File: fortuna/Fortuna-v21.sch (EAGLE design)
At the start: 33 parts, among them J1 9V, M1 MOTOR20MM, M2 MOTOR20MM, Q1 600mA/40V, Q2 600mA/40V, U2 OPA2344, U3 OPA2344

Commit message: Design board layout for Fortuna - v2.1
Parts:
- removed B1: ARDUINO_UNO_R3, SparkFun-Boards:ARDUINO_UNO_R3
- removed U3: OPA2344, Texas Instruments_By_element14_Batch_1:OPA2343UA
- added G1: AB9V, battery:AB9V
- added J2: GND, SparkFun-Connectors:CONN_01
- added J3: A0, SparkFun-Connectors:CONN_01
- added J4: A3, SparkFun-Connectors:CONN_01
- added J5: A5, SparkFun-Connectors:CONN_01
- added J6: D2, SparkFun-Connectors:CONN_01
- added J7: *D5, SparkFun-Connectors:CONN_01
- added J8: *D10, SparkFun-Connectors:CONN_01
- added J9: VIN, SparkFun-Connectors:CONN_01
- added U1: OPA2344, TexasInstruments:OPA2277PA
- D3: value LLED -> LLED_RED; device SparkFun-LED:LED3MM -> SparkFun-LED:LED5MM
- D4: value RLED -> RLED_RED; device SparkFun-LED:LED3MM -> SparkFun-LED:LED5MM
- J1: value 9V -> 5V; device SparkFun-Connectors:BC9VPC -> SparkFun-Connectors:CONN_01
- M1, M2: device SparkFun-Electromechanical:MOTOR10MM -> SparkFun-Connectors:CONN_02
- Q1, Q2: value 600mA/40V -> PN2222A; device SparkFun-DiscreteSemi:TRANS_NPN-P2N2222A -> Adafruit:2N2222
- U2: device Texas Instruments_By_element14_Batch_1:OPA2343UA -> TexasInstruments:OPA2277PA
- renumbered C3 to C1
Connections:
- removed net *D11: B1.*D11
- removed net *D3: B1.*D3
- removed net *D6: B1.*D6
- removed net *D9: B1.*D9
- removed net 3.3V: B1.3.3V
- removed net A1: B1.A1
- removed net A2: B1.A2
- removed net A4: B1.A4
- removed net AREF: B1.AREF
- removed net D0(RX): B1.D0
- removed net D1(TX): B1.D1
- removed net D12: B1.D12
- removed net D13: B1.D13
- removed net D4: B1.D4
- removed net D7: B1.D7
- removed net D8: B1.D8
- removed net IOREF: B1.IOREF
- removed net MISO: B1.MISO
- removed net MOSI: B1.MOSI
- removed net RESET: B1.!RESET!@1, B1.!RESET!@2
- removed net SCK: B1.SCK
- removed net SCL: B1.SCL
- removed net SDA: B1.SDA
- removed net VCC: B1.VCC
- net *D10: now also J8.1; no longer B1.*D10
- net *D5: now also J7.1; no longer B1.*D5
- net +LPHOTO: now also U1.+IN_A; no longer U2.+IN_A
- net +MIC: now also U1.+IN_B; no longer U2.+IN_B
- net +RPHOTO: now also U2.+IN_A; no longer U3.+IN_A
- net -LPHOTO: now also U1.-IN_A; no longer U2.-IN_A
- net -MIC: now also U1.-IN_B; no longer U2.-IN_B
- net -RPHOTO: now also U2.-IN_A; no longer U3.-IN_A
- net 5V: now also J1.1, U1.V+; no longer B1.5V, U3.V+
- net A0: now also J3.1, U1.OUT_A; no longer B1.A0, U2.OUT_A
- net A3: now also J4.1, U1.OUT_B; no longer B1.A3, U2.OUT_B
- net A5: now also J5.1, U2.OUT_A; no longer B1.A5, U3.OUT_A
- net D2: now also J6.1, U2.+IN_B; no longer B1.D2, U3.+IN_B
- net GND: now also G1.-, J2.1, U1.V-; no longer B1.GND, B1.GND@0, B1.GND@1, B1.GND@2, J1.V-, U3.V-
- net N$10: now also M1.2; no longer M1.-
- net N$12: now also M2.2; no longer M2.-
- net OUT_BUZZER: now also U2.-IN_B, U2.OUT_B; no longer U3.-IN_B, U3.OUT_B
- net VIN: now also G1.+, J9.1, M1.1, M2.1; no longer B1.VIN, J1.V+, M1.+, M2.+
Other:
- note added: "2.1"
- note removed: "2.0"
- moved on the sheet: U2

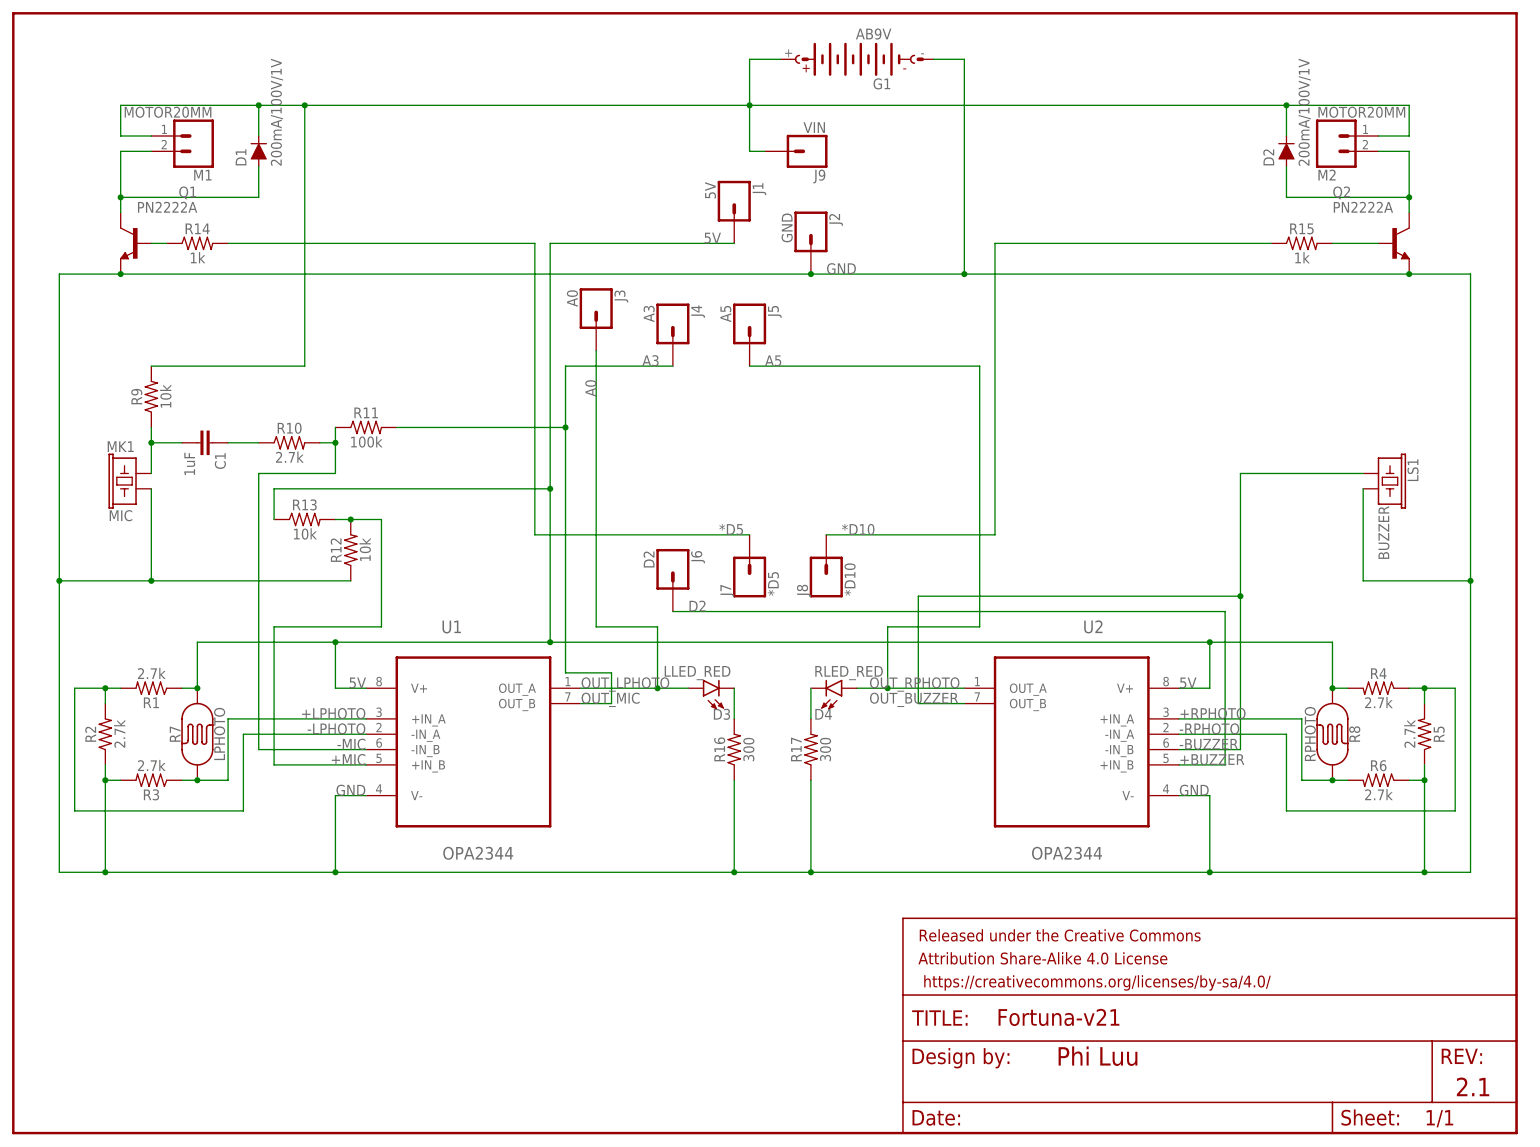
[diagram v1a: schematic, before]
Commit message: Merge two OPA2344's into one OPA4344 & Add SPDT power switch
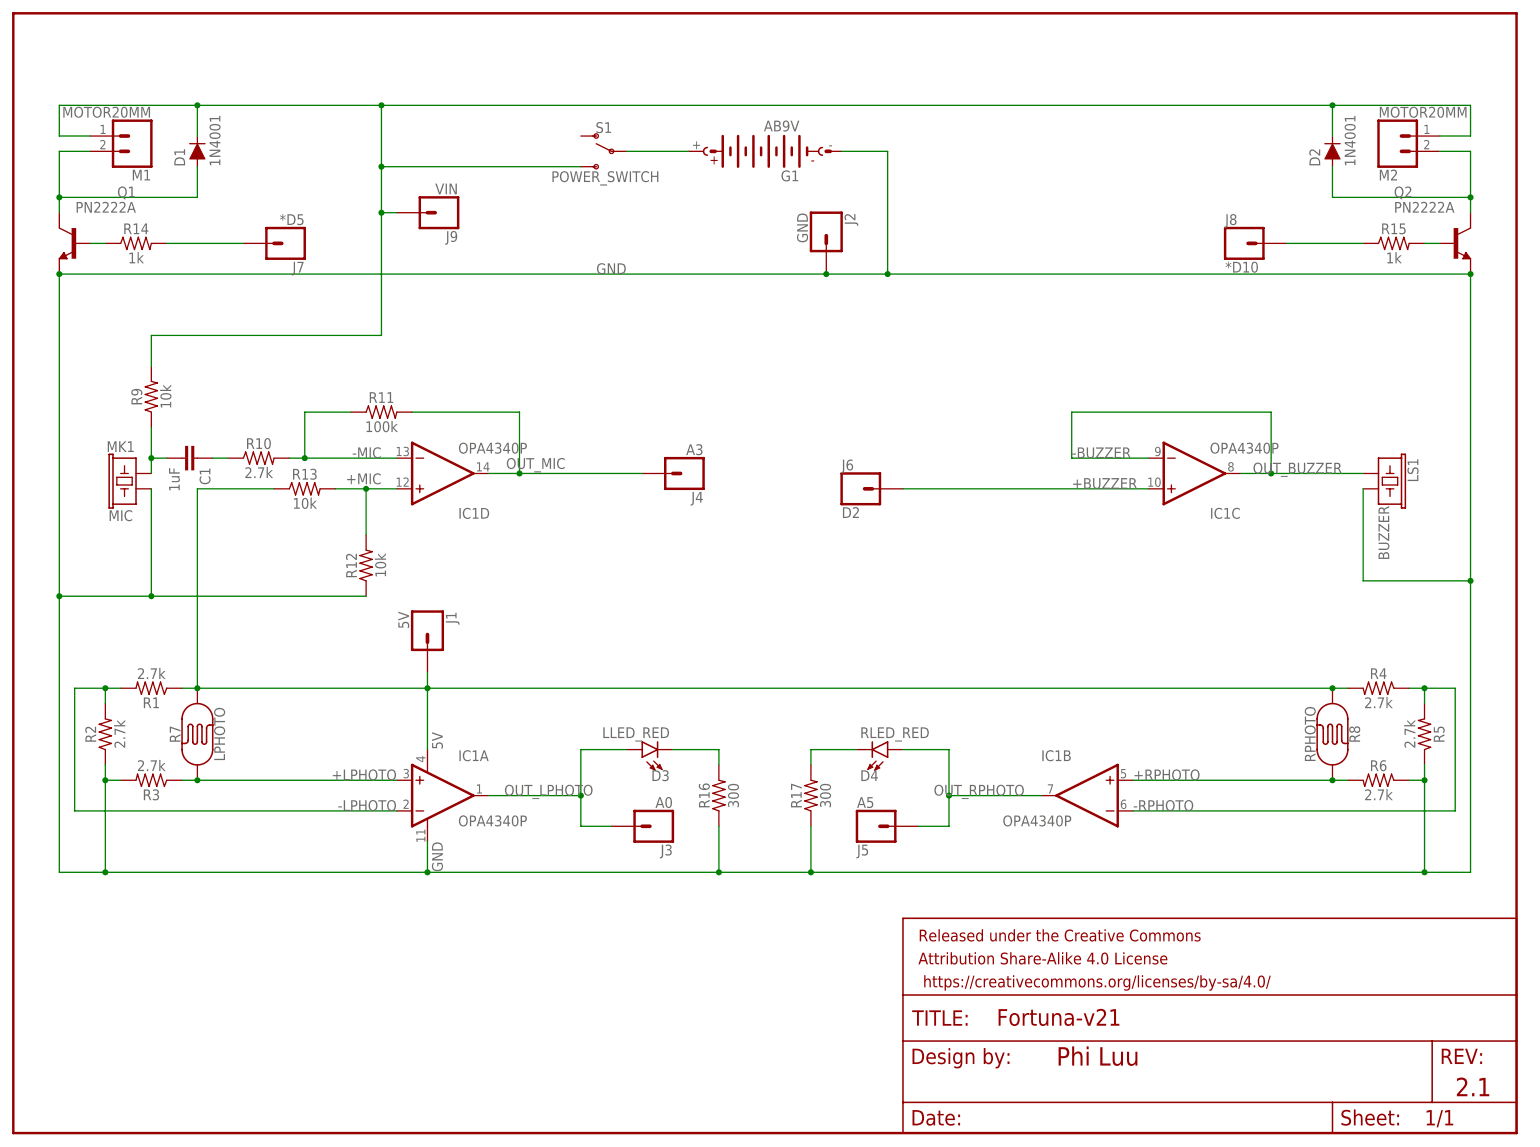
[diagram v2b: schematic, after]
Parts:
- removed U1, U2: OPA2344, TexasInstruments:OPA2277PA
- added IC1: OPA4340P, burr-brown:OPA4340P
- added S1: POWER_SWITCH, SparkFun-Switches:SWITCH-SPDT-PTH-11.6X4.0MM
- D1, D2: value 200mA/100V/1V -> 1N4001
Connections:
- net *D10 renamed OUT_RMOTOR
- net *D5 renamed OUT_LMOTOR
- removed net A0: D3.A, J3.1, U1.OUT_A
- removed net A3: J4.1, R11.2, U1.OUT_B
- removed net A5: D4.A, J5.1, U2.OUT_A
- new net 9V: G1.+, S1.P
- new net OUT_LPHOTO: D3.A, IC1A.OUT, J3.1
- new net OUT_MIC: IC1D.OUT, J4.1, R11.2
- new net OUT_RPHOTO: D4.A, IC1B.OUT, J5.1
- net +LPHOTO: now also IC1A.+IN; no longer U1.+IN_A
- net +MIC: now also IC1D.+IN; no longer U1.+IN_B
- net +RPHOTO: now also IC1B.+IN; no longer U2.+IN_A
- net -LPHOTO: now also IC1A.-IN; no longer U1.-IN_A
- net -MIC: now also IC1D.-IN; no longer U1.-IN_B
- net -RPHOTO: now also IC1B.-IN; no longer U2.-IN_A
- net 5V: now also IC1A.V+; no longer U1.V+, U2.V+
- net D2: now also IC1C.+IN; no longer U2.+IN_B
- net GND: now also IC1A.V-; no longer U1.V-, U2.V-
- net OUT_BUZZER: now also IC1C.-IN, IC1C.OUT; no longer U2.-IN_B, U2.OUT_B
- net VIN: now also S1.S; no longer G1.+
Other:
- note removed: "OUT_LPHOTO"
- note removed: "OUT_MIC"
- note removed: "OUT_RPHOTO"
- moved on the sheet: C1, D1, D2, D3, D4, G1, J1, J2, J3, J4, J5, J6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

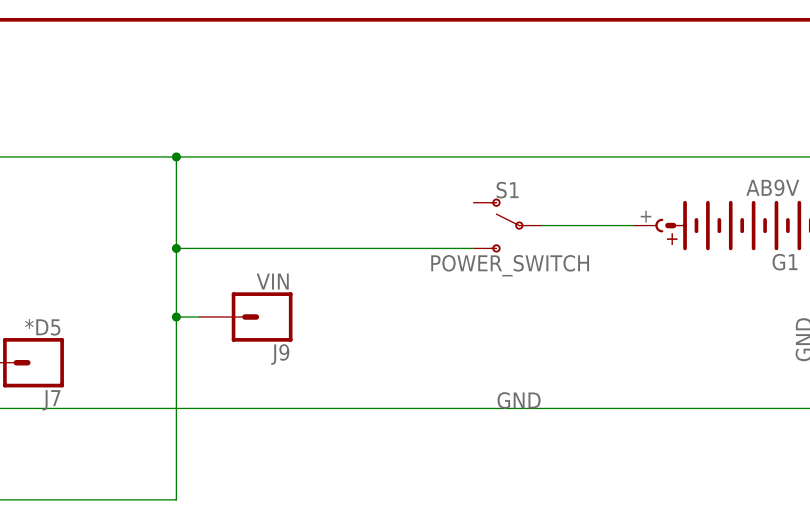
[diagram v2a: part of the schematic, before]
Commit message: Change pin position SPDT slide switch
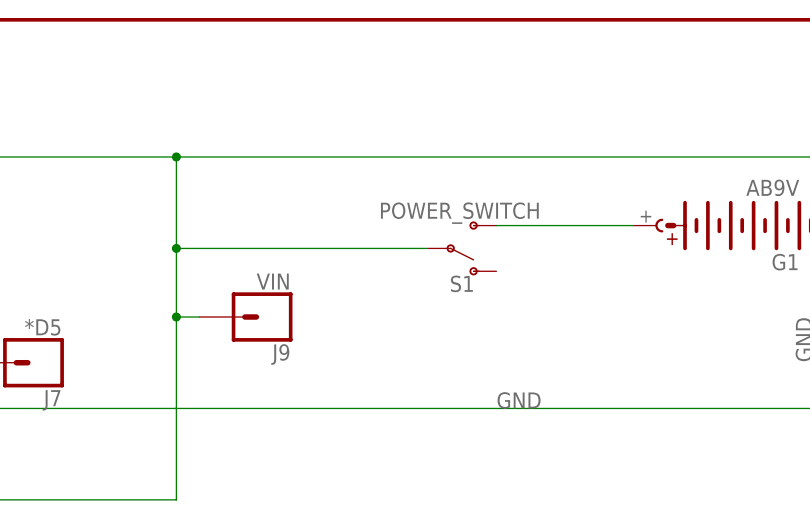
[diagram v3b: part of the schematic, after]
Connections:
- net 9V: now also S1.S; no longer S1.P
- net VIN: now also S1.P; no longer S1.S
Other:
- moved on the sheet: S1
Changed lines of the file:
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@@
 <instance part="IC1" gate="C" x="195.58" y="109.22" rot="MR180"/>
 <instance part="IC1" gate="D" x="71.12" y="109.22" rot="MR180"/>
-<instance part="S1" gate="1" x="99.06" y="162.56" rot="MR0"/>
+<instance part="S1" gate="1" x="91.44" y="160.02" rot="MR180"/>
 </instances>
 <busses>
@@
 <wire x1="60.96" y1="132.08" x2="60.96" y2="152.4" width="0.1524" layer="91"/>
 <wire x1="60.96" y1="152.4" x2="60.96" y2="160.02" width="0.1524" layer="91"/>
-<wire x1="60.96" y1="160.02" x2="93.98" y2="160.02" width="0.1524" layer="91"/>
-<pinref part="S1" gate="1" pin="S"/>
-<wire x1="60.96" y1="160.02" x2="60.96" y2="170.18" width="0.1524" layer="91"/>
-<junction x="60.96" y="160.02"/>
 <junction x="60.96" y="170.18"/>
 <pinref part="J9" gate="G$1" pin="1"/>
+<wire x1="60.96" y1="160.02" x2="60.96" y2="170.18" width="0.1524" layer="91"/>
 <wire x1="60.96" y1="152.4" x2="63.5" y2="152.4" width="0.1524" layer="91"/>
 <junction x="60.96" y="152.4"/>
+<pinref part="S1" gate="1" pin="P"/>
+<wire x1="88.9" y1="160.02" x2="60.96" y2="160.02" width="0.1524" layer="91"/>
+<junction x="60.96" y="160.02"/>
 </segment>
 </net>
@@
 </segment>
 </net>
-<net name="9V" class="1">
+<net name="9V" class="0">
 <segment>
 <pinref part="G1" gate="G$1" pin="+"/>
-<pinref part="S1" gate="1" pin="P"/>
-<wire x1="111.76" y1="162.56" x2="101.6" y2="162.56" width="0.1524" layer="91"/>
-</segment>
-</net>
+<pinref part="S1" gate="1" pin="S"/>
+<wire x1="111.76" y1="162.56" x2="96.52" y2="162.56" width="0.1524" layer="91"/>
+</segment>
+</net>

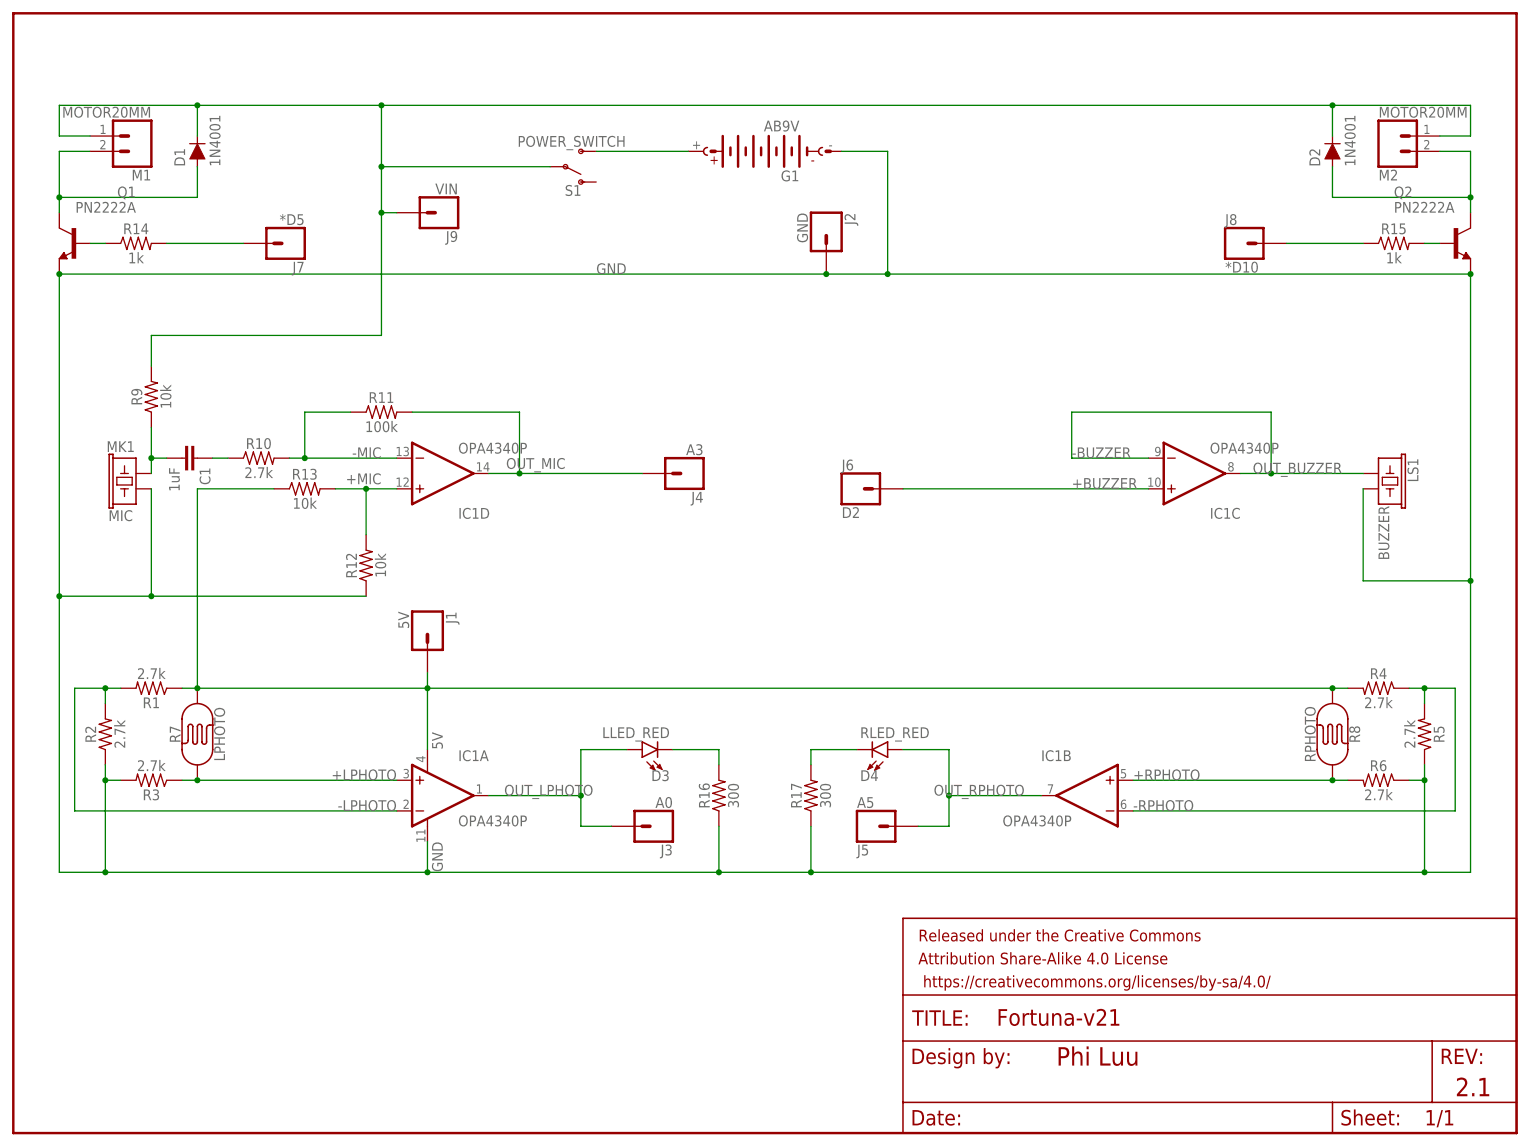
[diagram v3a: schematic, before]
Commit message: Add GND to RATSNEST
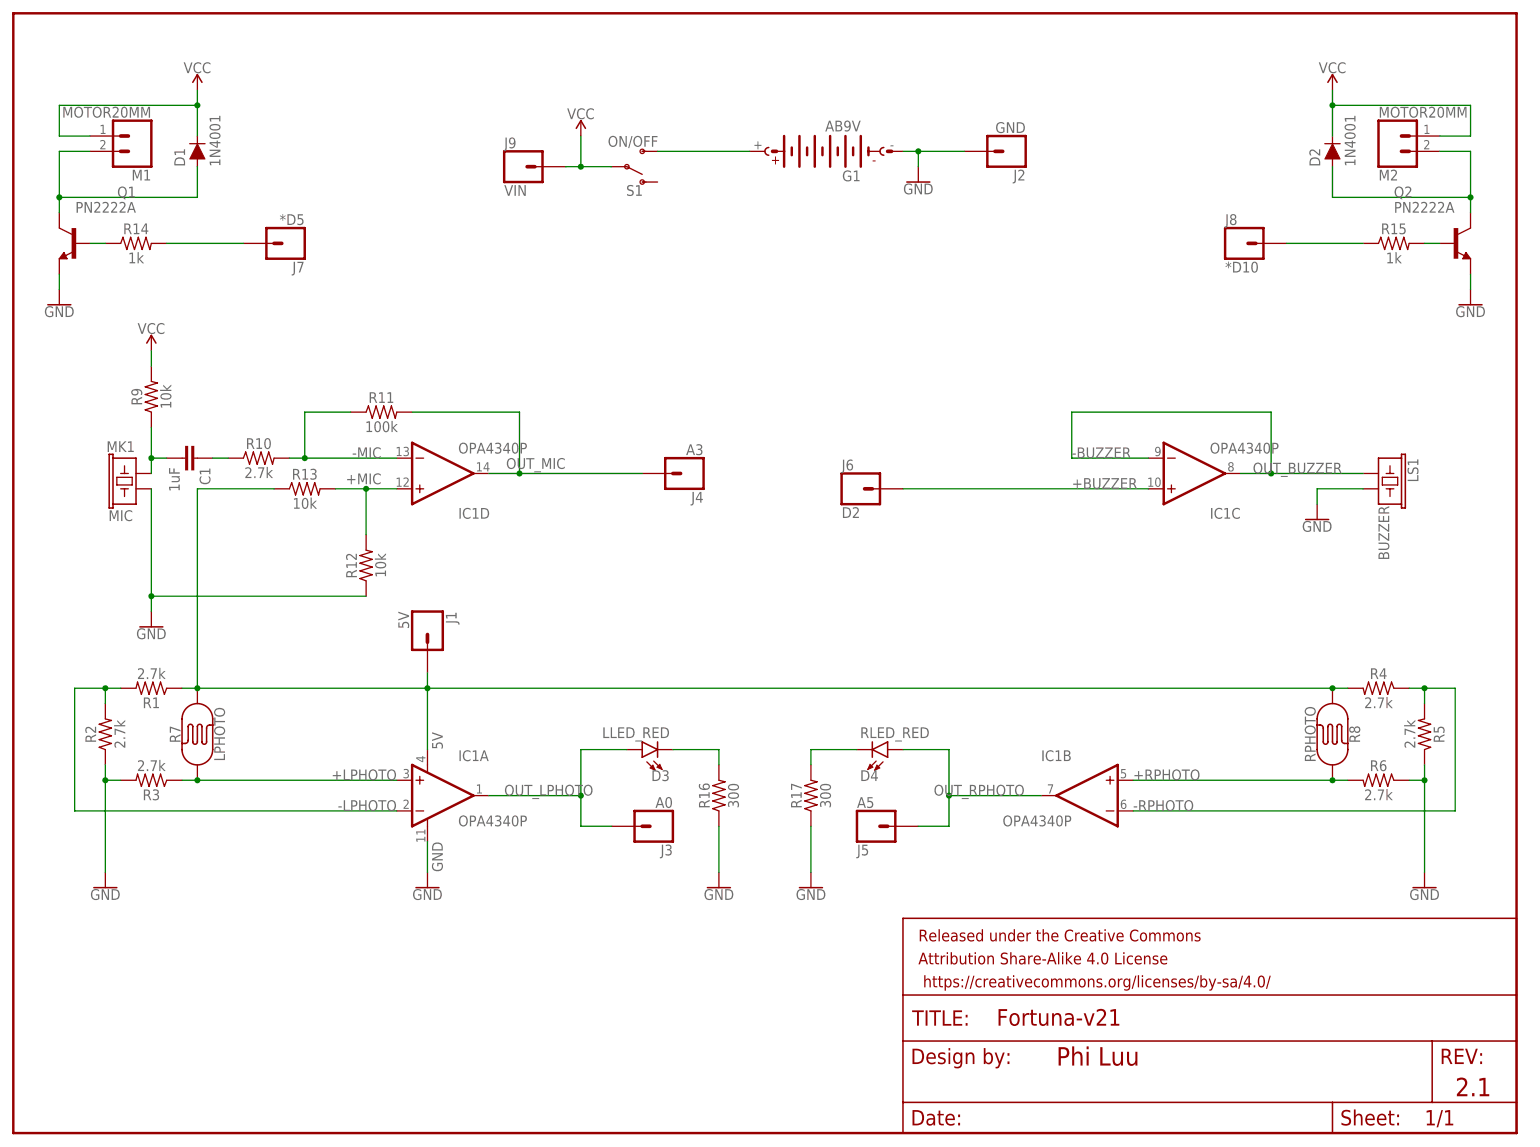
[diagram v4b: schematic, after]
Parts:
- D1, D2: device SparkFun-DiscreteSemi:DIODE-1N4148 -> SparkFun-DiscreteSemi:DIODE-PTH
- S1: value POWER_SWITCH -> ON/OFF
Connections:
- net VIN renamed VCC
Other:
- moved on the sheet: G1, J2, J9, S1
